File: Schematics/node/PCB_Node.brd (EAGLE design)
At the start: 25.7 x 37.5 mm, 19 parts, among them U1 ATMEGA328P, U2 MAX485CSA+, U3 MCP1824ST-3302E/DB

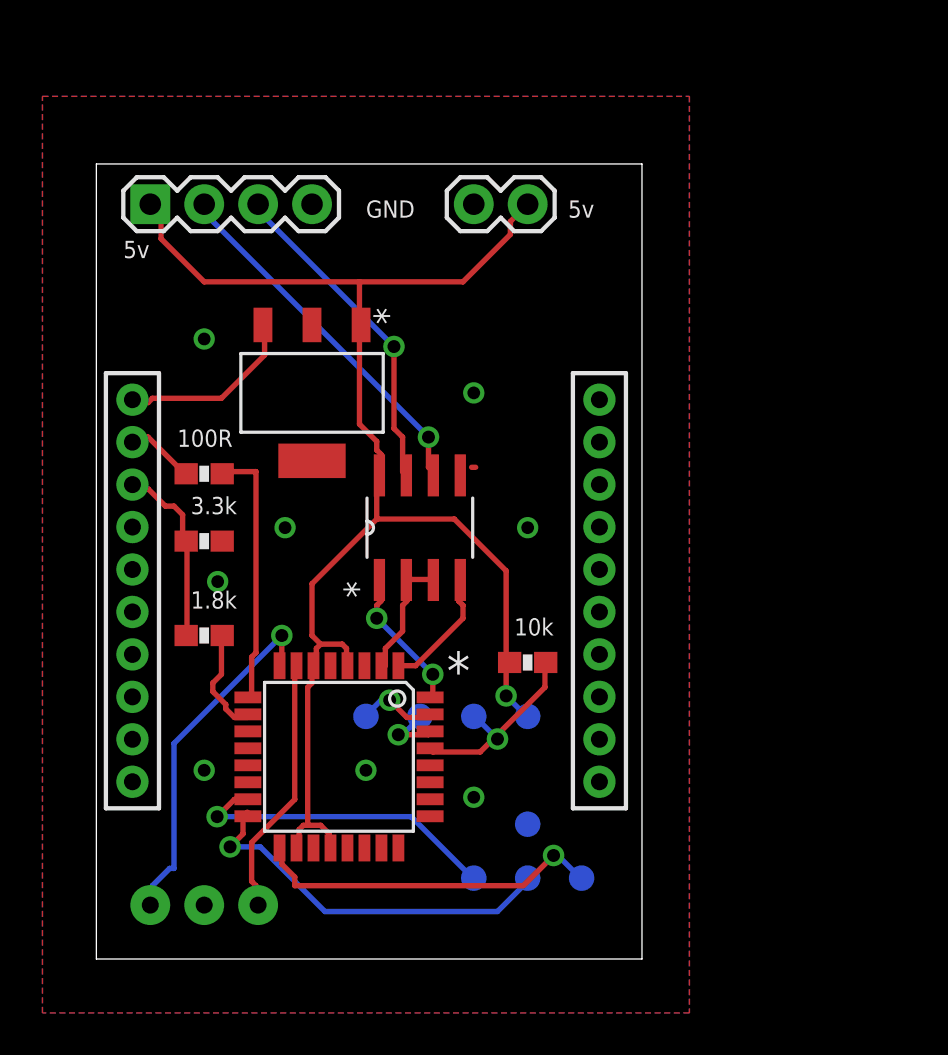
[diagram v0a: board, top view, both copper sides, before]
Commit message: PCB updates
changed sensor PCB to 3.0
changed Node PCB to 2.0 and parts list to go with it (Sach, can you
look over the schematic, board, and parts list that I have so far to
make sure I have everything correct?)
added Base Station PCB 0.5
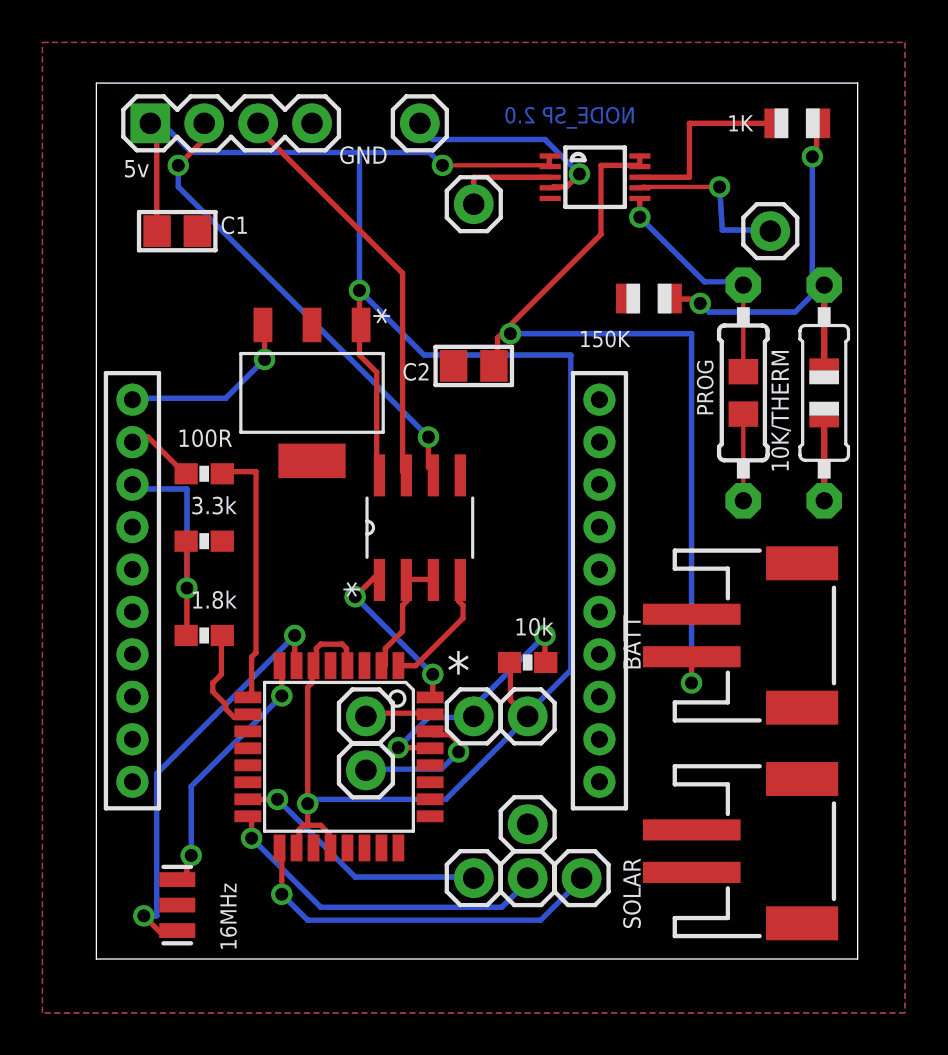
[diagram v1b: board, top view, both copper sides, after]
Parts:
- removed TP1, TP2, TP4, TP5, TP6, TP7, TP8, TP9: PTR1TP12R, testpad:TP12R
- removed Y1: (no value), SparkFun-FreqCtrl:RESONATOR-PTH
- added BATT: BATT_IN_JST, microbuilder:JSTPH2
- added C1, C2: (no value), microbuilder:0805
- added JP10, JP11, JP12, JP3, JP4, JP5, JP6, JP7, JP8, JP9: M01PTH, SparkFun-Connectors:1X01
- added R3: 1K, adafruit:R0805
- added R6: 150K, adafruit:R0805
- added R7: PROG, microbuilder:0805-THM
- added R8: 10K/THERM, adafruit:0805-THM
- added SOLAR: Solar_IN, microbuilder:JSTPH2
- added U4: (no value), microbuilder:MSOP10
- added Y2: 16MHz, SparkFun-FreqCtrl:RESONATOR-SMD
- JP2: value M02PTH -> M01PTH; device SparkFun-Connectors:1X02 -> SparkFun-Connectors:1X01
- moved JP2 29.2 mm to (20.3, 6.35), turned to 0 degrees
- moved JP1 3.81 mm to (2.54, 39.4)
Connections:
- new net N$10: JP12.1, U4.4
- new net N$11: JP11.1, U4.7
- new net N$19: BATT.2, C2.1, U4.10, U4.9
- new net N$3: R7.2, U4.6
- new net N$5: R3.1, U4.8
- new net N$7: R3.2, R6.2, R8.2
- new net N$8: C1.2
- new net N$9: JP10.1, U4.3
- net 1: now also JP8.1; no longer TP4.TP
- net 3: now also JP7.1; no longer TP2.TP
- net 4: now also JP9.1; no longer TP5.TP
- net GND: now also BATT.1, C2.2, JP2.1, R6.1, R7.1, R8.1, SOLAR.1, U4.5, Y2.2; no longer JP2.2, TP7.TP, Y1.2
- net N$12: now also Y2.3; no longer Y1.3
- net N$13: now also Y2.1; no longer Y1.1
- net N$15: now also JP4.1; no longer TP8.TP
- net N$16: now also JP5.1; no longer TP9.TP
- net RST: now also JP6.1; no longer TP1.TP
- net VCC: now also C1.1, JP3.1, U4.1, U4.2; no longer JP2.1, TP6.TP
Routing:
- net N$19: track 0.00 -> 40.4 mm, vias 0 -> 2
- net VCC: track 70.1 -> 99.6 mm, vias 1 -> 3
- net N$7: track 0.00 -> 16.3 mm, vias 0 -> 2
- net N$10: track 0.00 -> 10.2 mm, vias 0 -> 1
- net N$5: track 0.00 -> 8.95 mm
- net N$11: track 0.00 -> 8.08 mm, vias 0 -> 1
- net N$13: track 12.3 -> 20.0 mm, vias 0 -> 2
- net N$3: track 0.00 -> 7.17 mm, vias 0 -> 1
- net N$9: track 0.00 -> 4.87 mm
- net N$23: track 17.2 -> 22.1 mm, vias 1 -> 2
- net N$12: track 16.9 -> 12.4 mm, vias 1 -> 2
- net N$24: track 15.7 -> 19.5 mm, vias 1 -> 0
- net N$16: track 3.00 -> 6.71 mm
- net N$2: track 8.85 -> 11.8 mm, vias 0 -> 1
- net 4: track 15.1 -> 12.2 mm
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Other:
- board size 25.7 x 37.5 mm -> 35.9 x 41.3 mm
- board text added: "NODE_SP 2.0"
- board text added: "PWR"
- board text added: "Stat 1"
- board text added: "Stat 2"

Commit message: Corrected Node PCB issues found by Sachleen for version 2.0
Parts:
- moved C1 36.6 mm to (24.1, 3.81), turned to 270 degrees
- moved JP3 2.84 mm to (19.1, 8.89)
- moved JP10 1.80 mm to (16.5, 34.3)
- moved JP12 1.27 mm to (16.5, 39.4)
- moved JP2 1.27 mm to (19.1, 6.35)
- moved JP4 1.27 mm to (11.4, 11.4)
- moved JP5 1.27 mm to (11.4, 8.89)
- moved JP6 1.27 mm to (19.1, 11.4)
- moved JP7 1.27 mm to (21.6, 3.81)
- moved JP8 1.27 mm to (19.1, 3.81)
- moved JP9 1.27 mm to (16.5, 3.81)
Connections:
- net N$8: now also SOLAR.2
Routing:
- net VCC: track 99.6 -> 114.0 mm, vias 3 -> 5
- net N$8: track 0.00 -> 4.44 mm
- net RST: track 12.1 -> 7.70 mm, vias 2 -> 0
- net N$13: track 20.0 -> 16.3 mm
- net RO: track 8.26 -> 11.3 mm
- net N$9: track 4.87 -> 7.41 mm
- net N$10: track 10.2 -> 8.87 mm
- net 1: track 16.2 -> 14.8 mm
- net N$16: track 6.71 -> 5.45 mm, vias 1 -> 0
- net 4: track 12.2 -> 10.9 mm
- net N$15: track 3.12 -> 4.37 mm
- net 3: track 17.7 -> 16.4 mm
- net N$23: track 22.1 -> 21.0 mm
- net DOUT: track 12.5 -> 11.8 mm, vias 0 -> 2
- net GND: track 0.00 -> 0.07 mm, vias 0 -> 1

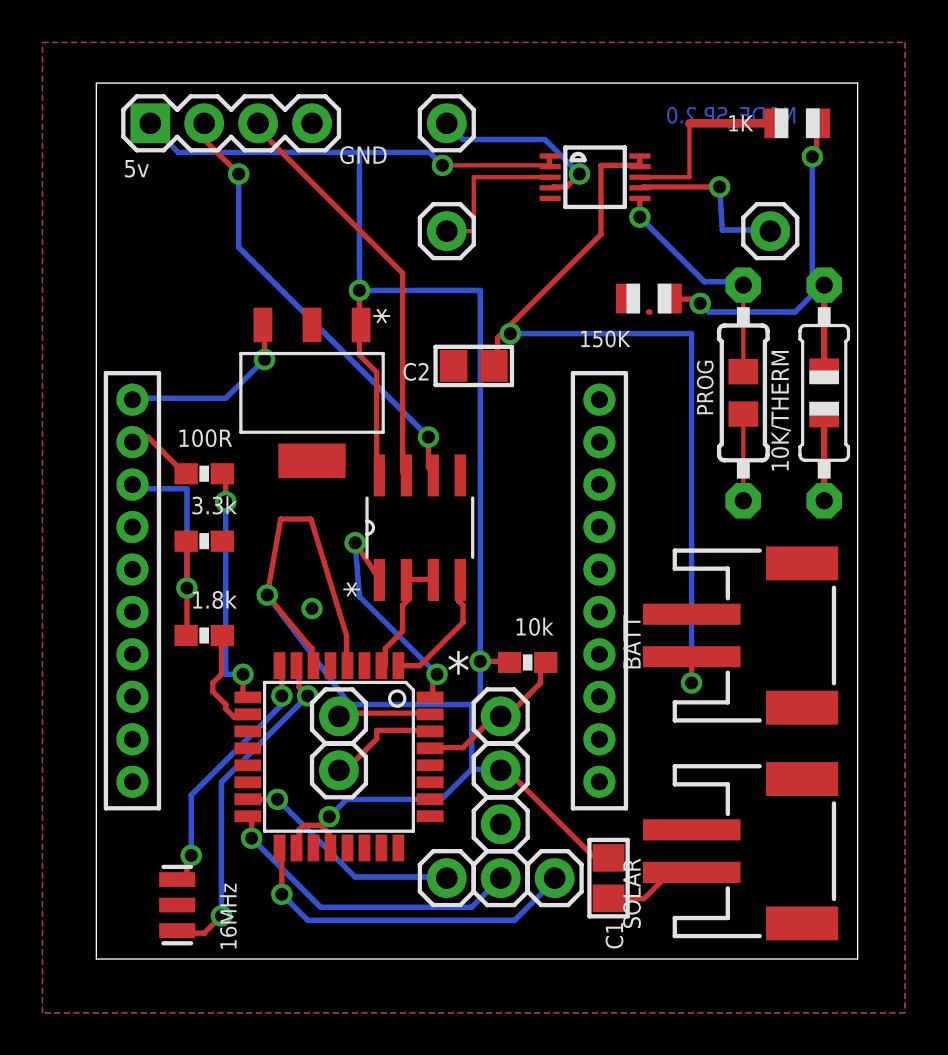
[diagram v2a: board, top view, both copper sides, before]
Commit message: Node Fixes
Made fixes to Node PCB.
- connected solar power to charging chip
- made power to battery and atmega from charging chip only
- rearranged board for these changes to work
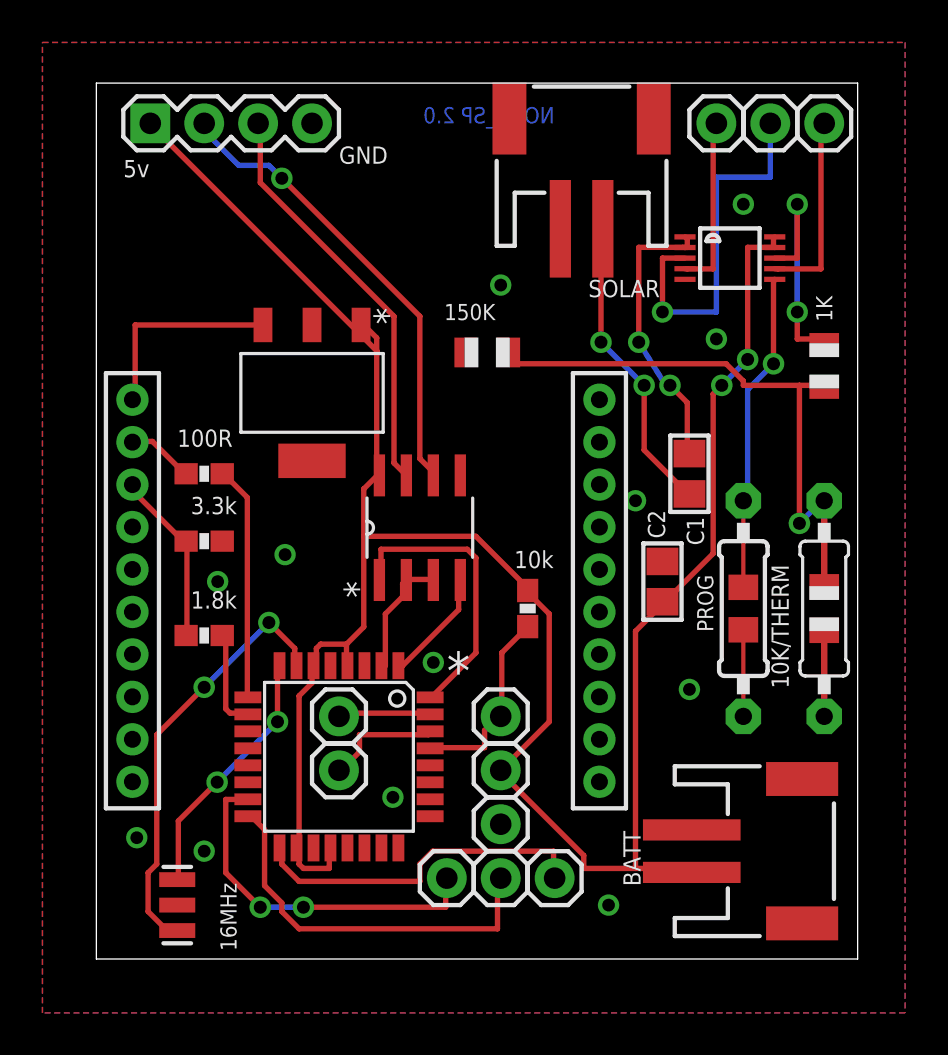
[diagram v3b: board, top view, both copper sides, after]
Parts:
- moved SOLAR 34.2 mm to (22.9, 38.1), turned to 0 degrees
- moved C1 19.4 mm to (27.9, 22.9)
- moved JP10 16.1 mm to (31.8, 39.4)
- moved C2 13.5 mm to (26.7, 17.8), turned to 90 degrees
- moved JP12 12.7 mm to (29.2, 39.4)
- moved R3 11.5 mm to (34.3, 27.9), turned to 270 degrees
- moved BATT 10.2 mm to (31.8, 5.08)
- moved R7 10.2 mm to (30.5, 16.5)
- moved R8 10.2 mm to (34.3, 16.5)
- moved R6 8.03 mm to (18.4, 28.6)
- moved U4 7.41 mm to (29.8, 33.0)
- moved JP11 5.68 mm to (34.3, 39.4)
- moved R5 2.54 mm to (20.3, 16.5), turned to 90 degrees
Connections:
- removed net N$19: BATT.2, C2.1, U4.10, U4.9
- new net N$14: C1.1, U4.1, U4.2
- net VCC: now also BATT.2, C2.1, U4.10, U4.9; no longer C1.1, U4.1, U4.2
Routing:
- net N$19: track 40.4 -> 0.00 mm, vias 2 -> 0
- net N$14: track 0.00 -> 13.5 mm, vias 0 -> 2
- net N$9: track 7.41 -> 17.6 mm, vias 0 -> 1
- net N$8: track 4.44 -> 14.3 mm, vias 0 -> 2
- net N$7: track 16.3 -> 24.0 mm, vias 2 -> 1
- net 4: track 10.9 -> 16.9 mm, vias 1 -> 2
- net N$13: track 16.3 -> 20.3 mm
- net N$3: track 7.17 -> 11.2 mm
- net N$2: track 11.8 -> 8.26 mm, vias 1 -> 0
- net VCC: track 114.0 -> 110.5 mm, vias 5 -> 2
- net 1: track 14.8 -> 18.2 mm, vias 1 -> 0
- net N$5: track 8.95 -> 11.5 mm, vias 0 -> 2
- net RO: track 11.3 -> 13.6 mm, vias 2 -> 0
- net RST: track 7.70 -> 9.15 mm
- net N$11: track 8.08 -> 9.10 mm, vias 1 -> 0
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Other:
- board text added: "St1"
- board text added: "St2"
- board text removed: "Stat 1"
- board text removed: "Stat 2"

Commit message: Node fixes
Corrected the c1 capacitor connected to solar power correctly
moved part names to locations where they will be read because of vias
blocking them
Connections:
- removed net N$14: C1.1, U4.1, U4.2
- net GND: now also C1.1
- net N$8: now also U4.1, U4.2
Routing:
- net N$8: track 14.3 -> 28.7 mm, vias 2 -> 0
- net N$14: track 13.5 -> 0.00 mm, vias 2 -> 0
- net N$9: track 17.6 -> 13.5 mm, vias 1 -> 2
- net N$5: track 11.5 -> 12.5 mm
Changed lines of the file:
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@@
 <text x="22.225" y="11.43" size="0.8128" layer="26" rot="MR0">RST</text>
 <text x="9.525" y="8.255" size="0.8128" layer="26" rot="MR0">RX</text>
-<text x="9.525" y="10.795" size="0.8128" layer="26" rot="MR0">TX</text>
+<text x="14.605" y="10.795" size="0.8128" layer="26" rot="MR0">TX</text>
 <text x="3.81" y="24.13" size="0.8128" layer="25">100R</text>
 <text x="4.445" y="20.955" size="0.8128" layer="25">3.3k</text>
@@
 <contactref element="Y2" pad="2"/>
 <contactref element="JP2" pad="1"/>
+<contactref element="C1" pad="1"/>
 <via x="1.905" y="5.715" extent="1-16" drill="0.6"/>
 <via x="5.08" y="5.08" extent="1-16" drill="0.6"/>
+<via x="13.97" y="7.62" extent="1-16" drill="0.6"/>
 <via x="24.13" y="2.54" extent="1-16" drill="0.6"/>
-<via x="27.94" y="12.7" extent="1-16" drill="0.6"/>
-<via x="13.97" y="7.62" extent="1-16" drill="0.6"/>
+<via x="33.02" y="5.08" extent="1-16" drill="0.6"/>
+<via x="27.94" y="11.43" extent="1-16" drill="0.6"/>
+<via x="23.495" y="6.35" extent="1-16" drill="0.6"/>
+<via x="15.875" y="13.97" extent="1-16" drill="0.6"/>
+<via x="8.89" y="19.05" extent="1-16" drill="0.6"/>
 <via x="5.715" y="17.78" extent="1-16" drill="0.6"/>
-<via x="8.89" y="19.05" extent="1-16" drill="0.6"/>
-<via x="25.4" y="21.59" extent="1-16" drill="0.6"/>
-<via x="19.05" y="31.75" extent="1-16" drill="0.6"/>
-<via x="29.21" y="29.21" extent="1-16" drill="0.6"/>
-<via x="30.48" y="35.56" extent="1-16" drill="0.6"/>
-<via x="15.875" y="13.97" extent="1-16" drill="0.6"/>
+<via x="3.81" y="21.59" extent="1-16" drill="0.6"/>
+<via x="20.32" y="22.86" extent="1-16" drill="0.6"/>
+<via x="31.75" y="24.13" extent="1-16" drill="0.6"/>
+<via x="5.08" y="26.67" extent="1-16" drill="0.6"/>
+<via x="2.54" y="34.29" extent="1-16" drill="0.6"/>
+<via x="15.24" y="35.56" extent="1-16" drill="0.6"/>
+<via x="22.86" y="30.48" extent="1-16" drill="0.6"/>
+<via x="26.67" y="36.83" extent="1-16" drill="0.6"/>
+<via x="33.02" y="36.83" extent="1-16" drill="0.6"/>
+<via x="26.67" y="26.67" extent="1-16" drill="0.6"/>
+<via x="25.4" y="22.86" extent="1-16" drill="0.6"/>
 </signal>
 <signal name="3">
@@
 <contactref element="U4" pad="8"/>
 <contactref element="R3" pad="1"/>
-<wire x1="33.02" y1="30.48" x2="33.02" y2="35.56" width="0.254" layer="16"/>
+<wire x1="31.75" y1="35.56" x2="33.02" y2="34.29" width="0.254" layer="1"/>
+<wire x1="31.75" y1="31.75" x2="31.75" y2="35.56" width="0.254" layer="16"/>
+<wire x1="33.02" y1="30.48" x2="31.75" y2="31.75" width="0.254" layer="16"/>
 <wire x1="33.02" y1="29.21" x2="33.02" y2="30.48" width="0.254" layer="1"/>
 <wire x1="34.29" y1="29.21" x2="33.02" y2="29.21" width="0.254" layer="1"/>
 <wire x1="34.29" y1="29.21" x2="34.29" y2="28.94" width="0.254" layer="1"/>
-<via x="33.02" y="35.56" extent="1-16" drill="0.6"/>
+<via x="31.75" y="35.56" extent="1-16" drill="0.6"/>
 <via x="33.02" y="30.48" extent="1-16" drill="0.6"/>
 <wire x1="31.9581" y1="33.02" x2="33.02" y2="33.02" width="0.254" layer="1"/>
-<wire x1="33.02" y1="33.02" x2="33.02" y2="35.56" width="0.254" layer="1"/>
+<wire x1="33.02" y1="33.02" x2="33.02" y2="34.29" width="0.254" layer="1"/>
 </signal>
 <signal name="N$7">
@@
 <wire x1="33.1216" y1="27.0256" x2="34.1376" y2="27.0256" width="0.254" layer="1"/>
 <wire x1="30.48" y1="27.2288" x2="30.48" y2="27.0256" width="0.254" layer="1"/>
-<wire x1="29.6672" y1="28.0416" x2="30.48" y2="27.2288" width="0.254" layer="1"/>
-<wire x1="19.5072" y1="28.0416" x2="29.6672" y2="28.0416" width="0.254" layer="1"/>
-<wire x1="19.5072" y1="28.448" x2="19.5072" y2="28.0416" width="0.254" layer="1"/>
+<wire x1="29.2608" y1="28.448" x2="30.48" y2="27.2288" width="0.254" layer="1"/>
+<wire x1="19.5072" y1="28.448" x2="29.2608" y2="28.448" width="0.254" layer="1"/>
 <wire x1="34.1376" y1="27.0256" x2="34.29" y2="26.94" width="0.254" layer="1"/>
 <wire x1="19.5072" y1="28.448" x2="19.415" y2="28.575" width="0.254" layer="1"/>
@@
 <contactref element="C1" pad="2"/>
 <contactref element="SOLAR" pad="2"/>
-<wire x1="25.8064" y1="23.9776" x2="27.8384" y2="21.9456" width="0.254" layer="1"/>
-<wire x1="25.8064" y1="27.0256" x2="25.8064" y2="23.9776" width="0.254" layer="1"/>
-<wire x1="23.7744" y1="29.0576" x2="25.8064" y2="27.0256" width="0.254" layer="16"/>
-<wire x1="23.7744" y1="34.3408" x2="23.7744" y2="29.0576" width="0.254" layer="1"/>
+<contactref element="U4" pad="2"/>
+<contactref element="U4" pad="1"/>
+<wire x1="27.8384" y1="33.9344" x2="27.8384" y2="33.528" width="0.254" layer="1"/>
+<wire x1="27.8384" y1="33.528" x2="27.7319" y2="33.52" width="0.254" layer="1"/>
+<wire x1="27.8384" y1="33.9344" x2="27.7319" y2="34.02" width="0.254" layer="1"/>
+<wire x1="23.9776" y1="34.1376" x2="27.6352" y2="34.1376" width="0.254" layer="1"/>
+<wire x1="23.9776" y1="34.3408" x2="23.9776" y2="34.1376" width="0.254" layer="1"/>
+<wire x1="27.6352" y1="34.1376" x2="27.7319" y2="34.02" width="0.254" layer="1"/>
+<wire x1="23.9776" y1="34.3408" x2="23.86" y2="34.4" width="0.254" layer="1"/>
+<wire x1="24.9936" y1="24.7904" x2="27.8384" y2="21.9456" width="0.254" layer="1"/>
+<wire x1="24.9936" y1="26.6192" x2="24.9936" y2="24.7904" width="0.254" layer="1"/>
+<wire x1="23.9776" y1="27.6352" x2="24.9936" y2="26.6192" width="0.254" layer="1"/>
+<wire x1="20.32" y1="27.6352" x2="23.9776" y2="27.6352" width="0.254" layer="1"/>
+<wire x1="20.1168" y1="27.432" x2="20.32" y2="27.6352" width="0.254" layer="1"/>
+<wire x1="18.4912" y1="27.432" x2="20.1168" y2="27.432" width="0.254" layer="1"/>
+<wire x1="18.4912" y1="29.464" x2="18.4912" y2="27.432" width="0.254" layer="1"/>
+<wire x1="20.7264" y1="31.6992" x2="18.4912" y2="29.464" width="0.254" layer="1"/>
+<wire x1="23.7744" y1="31.6992" x2="20.7264" y2="31.6992" width="0.254" layer="1"/>
+<wire x1="23.7744" y1="34.3408" x2="23.7744" y2="31.6992" width="0.254" layer="1"/>
 <wire x1="27.8384" y1="21.9456" x2="27.94" y2="21.91" width="0.254" layer="1"/>
 <wire x1="23.7744" y1="34.3408" x2="23.86" y2="34.4" width="0.254" layer="1"/>
-<via x="25.8064" y="27.0256" extent="1-16" drill="0.6096"/>
-<via x="23.7744" y="29.0576" extent="1-16" drill="0.6096"/>
 </signal>
 <signal name="N$9">
 <contactref element="JP10" pad="1"/>
 <contactref element="U4" pad="3"/>
-<wire x1="27.7319" y1="33.02" x2="26.67" y2="33.02" width="0.254" layer="1"/>
-<wire x1="26.67" y1="33.02" x2="26.67" y2="30.48" width="0.254" layer="1"/>
-<via x="26.67" y="30.48" extent="1-16" drill="0.6"/>
-<wire x1="31.75" y1="39.37" x2="31.75" y2="36.83" width="0.254" layer="16"/>
-<wire x1="31.75" y1="36.83" x2="29.21" y2="36.83" width="0.254" layer="16"/>
-<wire x1="29.21" y1="36.83" x2="29.21" y2="30.48" width="0.254" layer="16"/>
-<wire x1="29.21" y1="30.48" x2="26.67" y2="30.48" width="0.254" layer="16"/>
+<wire x1="25.4" y1="33.02" x2="27.7319" y2="33.02" width="0.254" layer="1"/>
+<wire x1="27.94" y1="35.56" x2="25.4" y2="33.02" width="0.254" layer="16"/>
+<wire x1="30.48" y1="35.56" x2="27.94" y2="35.56" width="0.254" layer="16"/>
+<wire x1="30.48" y1="39.37" x2="30.48" y2="35.56" width="0.254" layer="1"/>
+<wire x1="31.75" y1="39.37" x2="30.48" y2="39.37" width="0.254" layer="1"/>
+<via x="25.4" y="33.02" extent="1-16" drill="0.6"/>
+<via x="30.48" y="35.56" extent="1-16" drill="0.6"/>
 </signal>
 <signal name="N$10">
@@
 <wire x1="34.1376" y1="39.2176" x2="34.29" y2="39.37" width="0.254" layer="1"/>
 </signal>
-<signal name="N$14">
-<contactref element="U4" pad="2"/>
-<contactref element="U4" pad="1"/>
-<contactref element="C1" pad="1"/>
-<wire x1="27.8384" y1="33.9344" x2="27.8384" y2="33.528" width="0.254" layer="1"/>
-<wire x1="27.8384" y1="33.528" x2="27.7319" y2="33.52" width="0.254" layer="1"/>
-<wire x1="27.8384" y1="33.9344" x2="27.7319" y2="34.02" width="0.254" layer="1"/>
-<wire x1="25.5524" y1="33.528" x2="27.6352" y2="33.528" width="0.254" layer="1"/>
-<wire x1="25.5524" y1="29.0576" x2="25.5524" y2="33.528" width="0.254" layer="1"/>
-<wire x1="26.8224" y1="27.0256" x2="25.5524" y2="29.0576" width="0.254" layer="16"/>
-<wire x1="27.0256" y1="27.0256" x2="26.8224" y2="27.0256" width="0.254" layer="16"/>
-<wire x1="27.8384" y1="26.2128" x2="27.0256" y2="27.0256" width="0.254" layer="1"/>
-<wire x1="27.8384" y1="23.9776" x2="27.8384" y2="26.2128" width="0.254" layer="1"/>
-<wire x1="27.6352" y1="33.528" x2="27.7319" y2="33.52" width="0.254" layer="1"/>
-<wire x1="27.8384" y1="23.9776" x2="27.94" y2="23.81" width="0.254" layer="1"/>
-<via x="25.5524" y="29.0576" extent="1-16" drill="0.6096"/>
-<via x="27.0256" y="27.0256" extent="1-16" drill="0.6096"/>
-</signal>
 <signal name="N$17">
